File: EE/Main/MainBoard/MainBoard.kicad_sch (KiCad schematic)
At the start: 0 parts

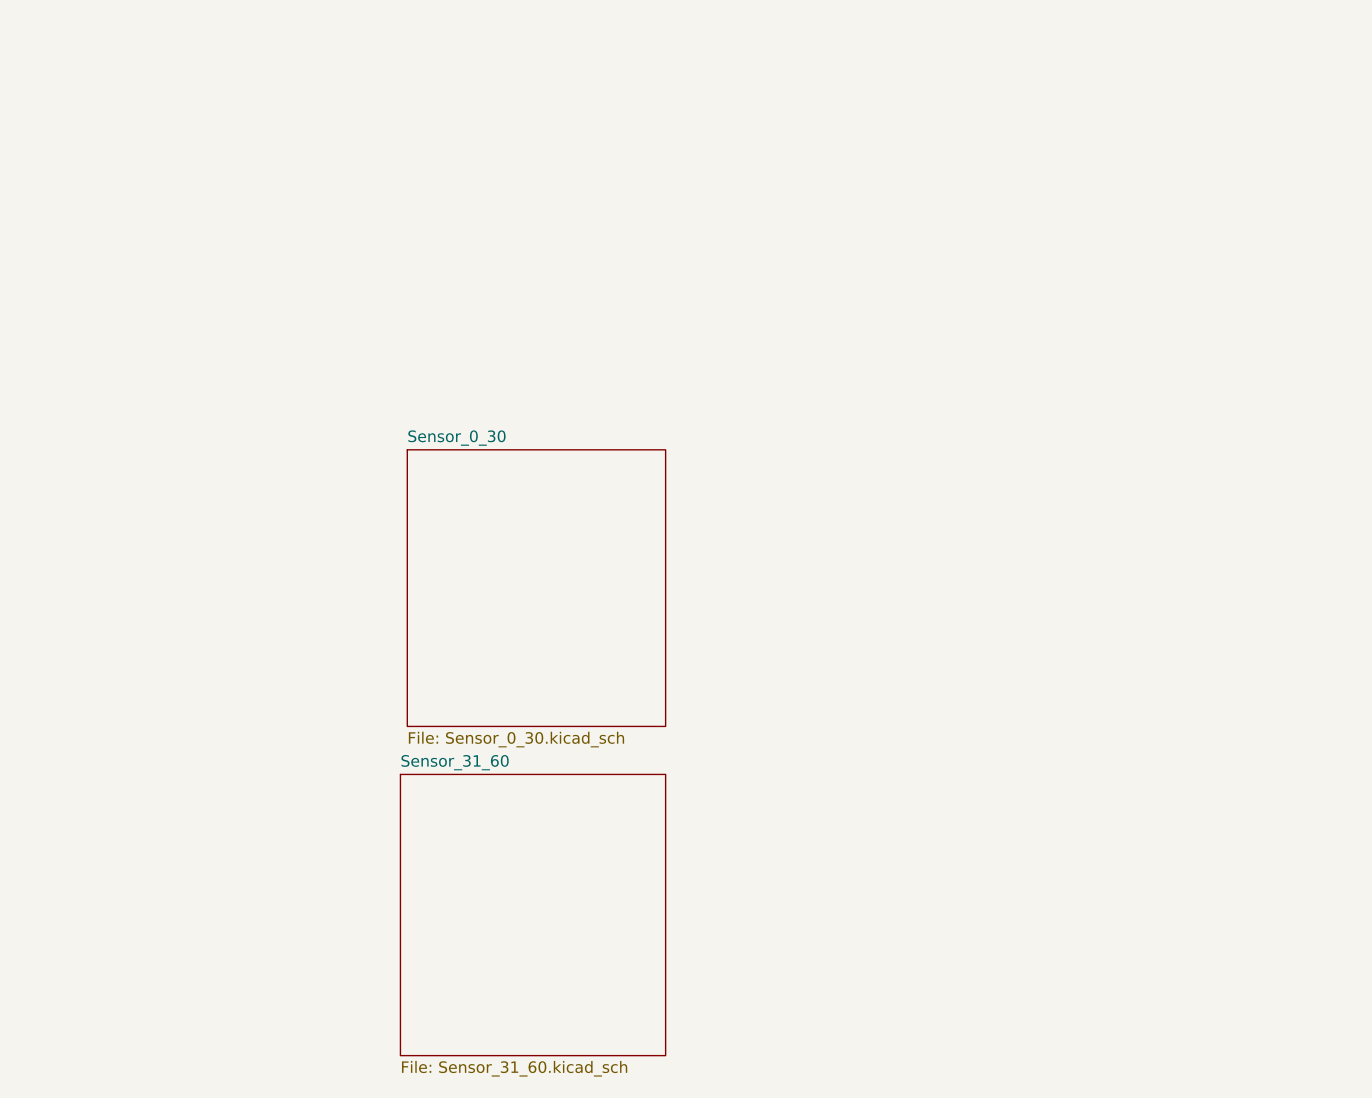
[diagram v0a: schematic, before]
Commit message: Sensors attached to mainboard
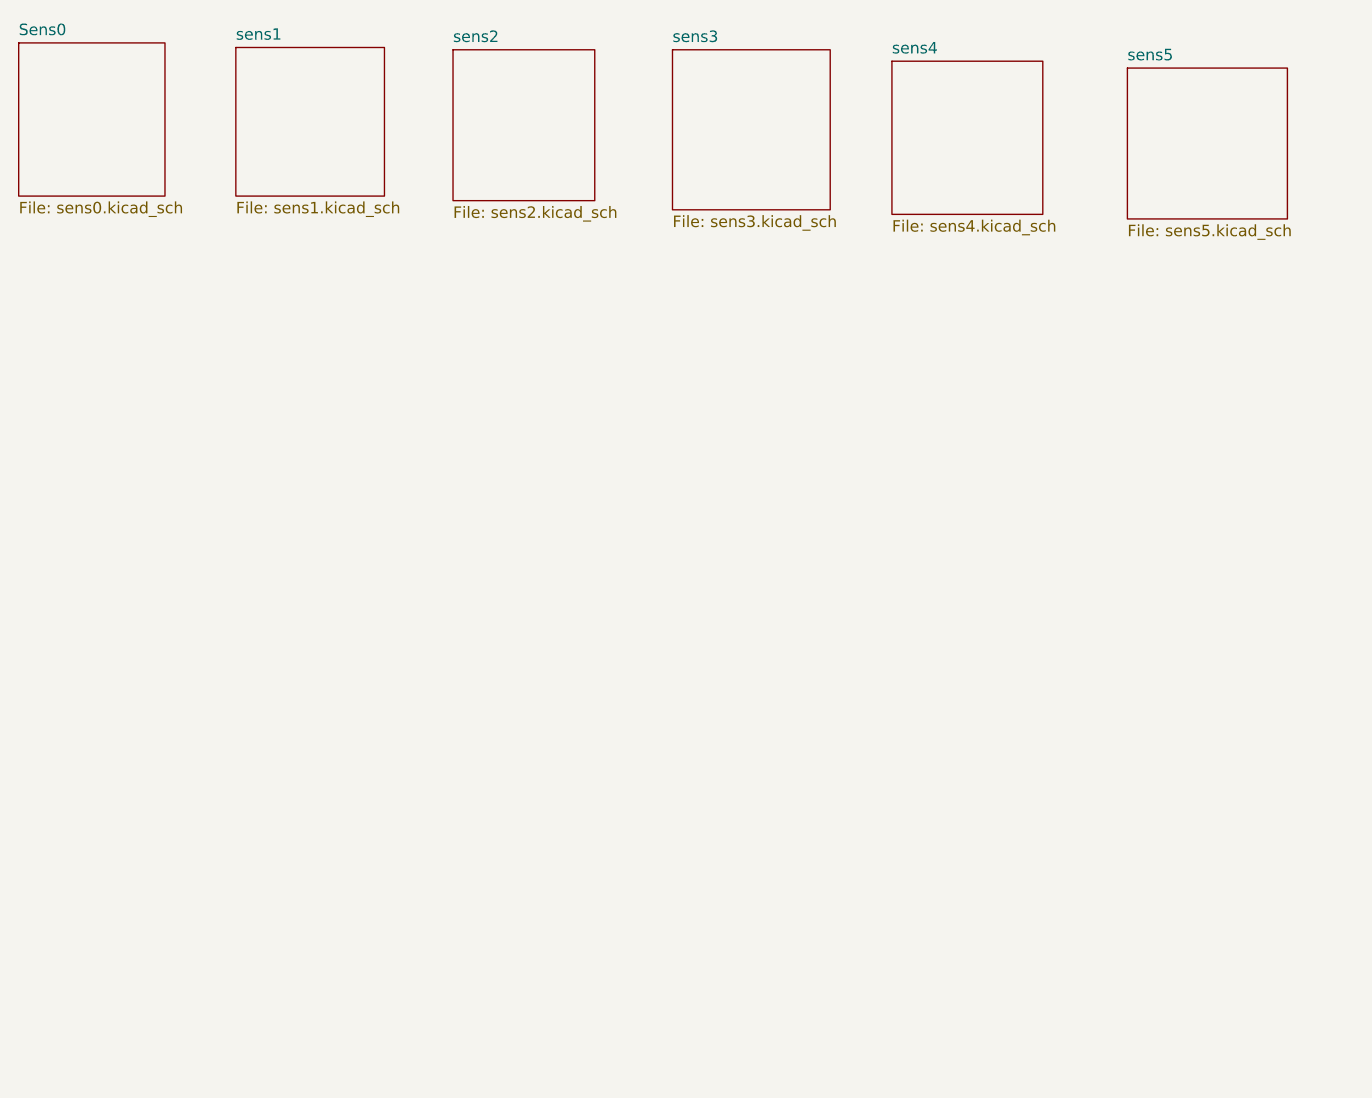
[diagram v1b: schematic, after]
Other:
- removed sheet Sensor_0_30
- removed sheet Sensor_31_60
- added sheet Sens0 (sens0.kicad_sch)
- added sheet sens1 (sens1.kicad_sch)
- added sheet sens2 (sens2.kicad_sch)
- added sheet sens3 (sens3.kicad_sch)
- added sheet sens4 (sens4.kicad_sch)
- added sheet sens5 (sens5.kicad_sch)

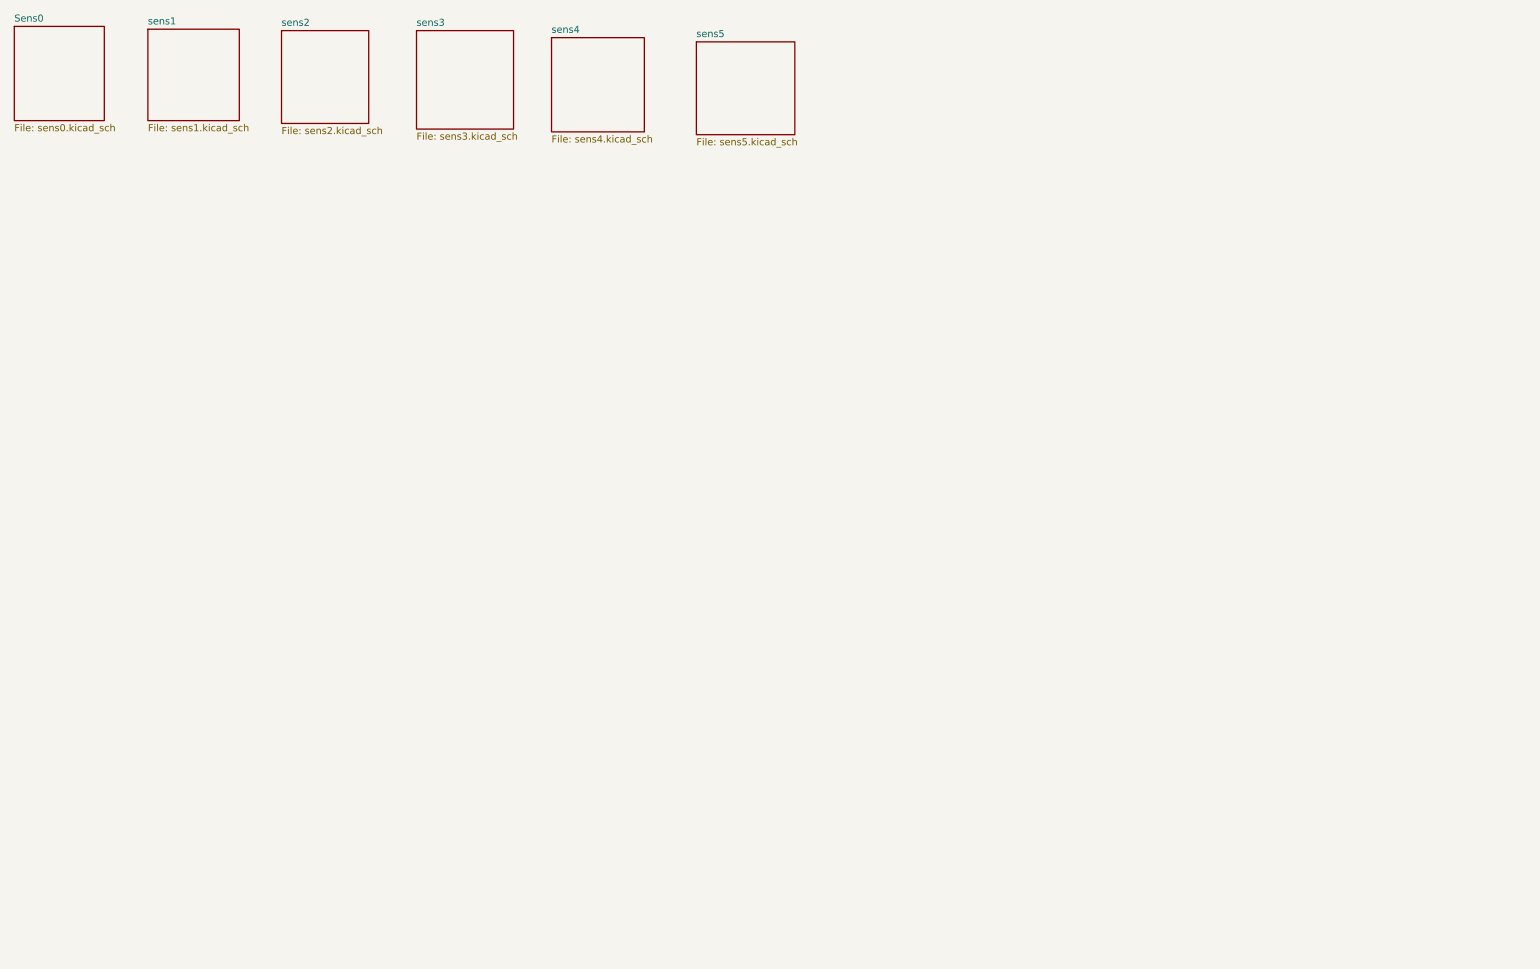
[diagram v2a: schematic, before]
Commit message: WIP - Moving Sensor to IO Expander
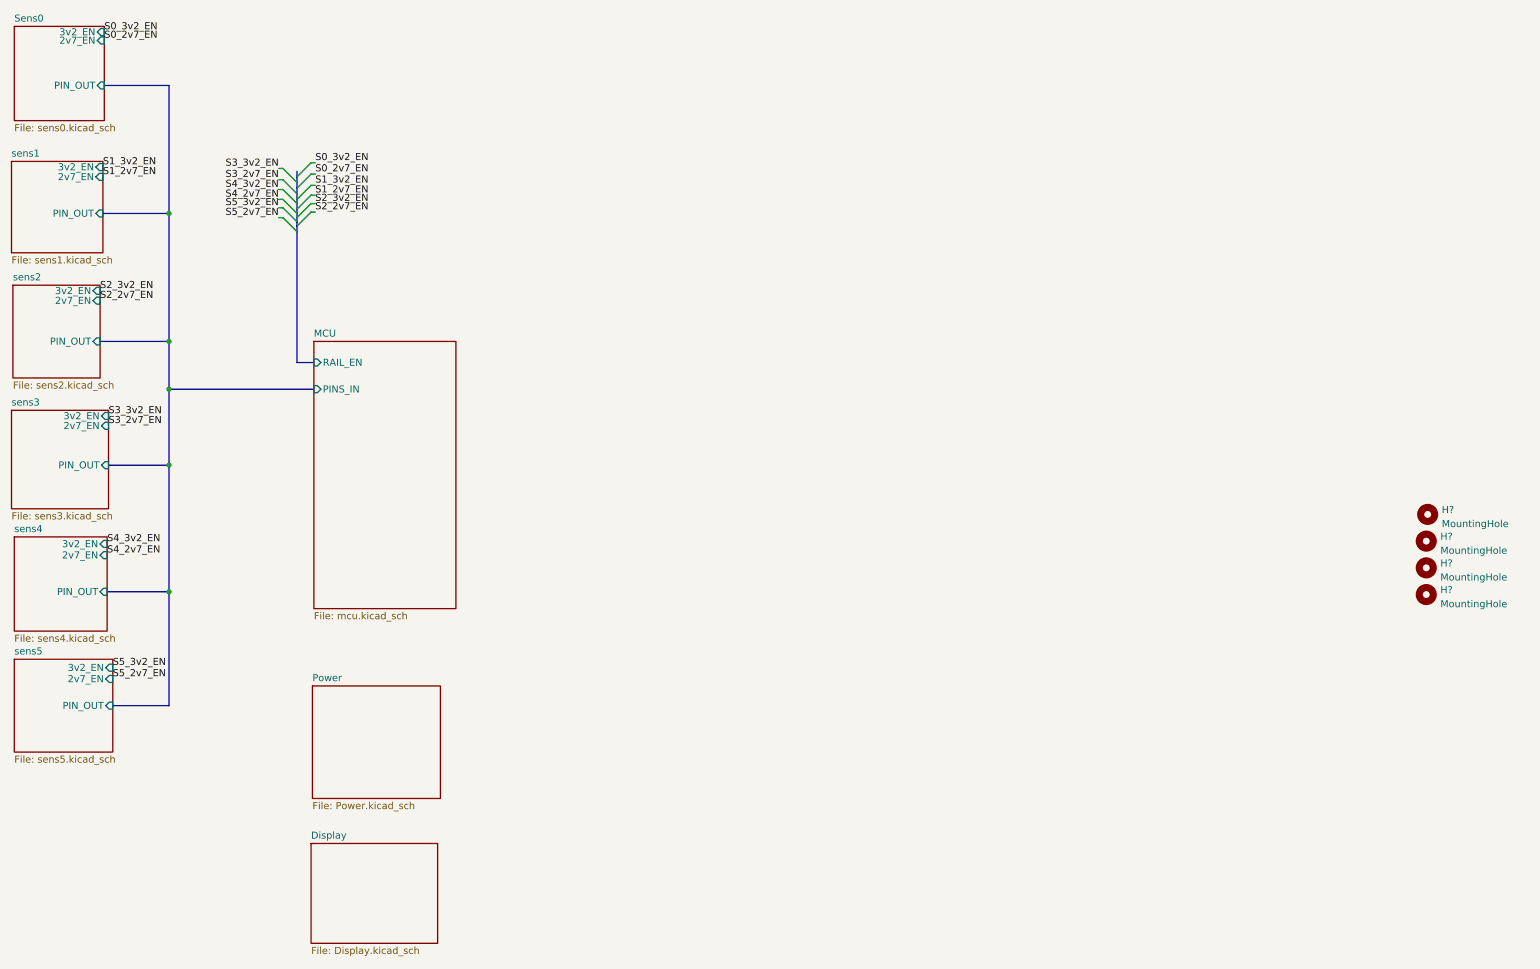
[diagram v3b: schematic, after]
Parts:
- added H? (x4): MountingHole, MountingHole:MountingHole_2.5mm, symbol Mechanical:MountingHole
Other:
- added sheet Display (Display.kicad_sch)
- added sheet MCU (mcu.kicad_sch)
- added sheet Power (Power.kicad_sch)
- sheet Sens0 ports: added 2v7_EN, 3v2_EN, PIN_OUT; removed none
- sheet sens1 ports: added 2v7_EN, 3v2_EN, PIN_OUT; removed none
- sheet sens2 ports: added 2v7_EN, 3v2_EN, PIN_OUT; removed none
- sheet sens3 ports: added 2v7_EN, 3v2_EN, PIN_OUT; removed none
- sheet sens4 ports: added 2v7_EN, 3v2_EN, PIN_OUT; removed none
- sheet sens5 ports: added 2v7_EN, 3v2_EN, PIN_OUT; removed none

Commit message: Updated layout, and placement for main board
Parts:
- gave numbers to parts that had none: 4
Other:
- sheet Display ports: added A_EN, B_EN, C_EN, D1_G_EN, D1_R_EN, D2_G_EN, D2_R_EN, D_EN, E_EN, F_EN, G_EN; removed none
- sheet MCU ports: added A_EN, B_EN, C_EN, D1_G_EN, D1_R_EN, D2_G_EN, D2_R_EN, D_EN, E_EN, F_EN, G_EN, SCL, SDA; removed PINS_IN, RAIL_EN
- sheet Sens0 ports: added SCL, SDA; removed 2v7_EN, 3v2_EN, PIN_OUT
- sheet sens1 ports: added SCL, SDA; removed 2v7_EN, 3v2_EN, PIN_OUT
- sheet sens2 ports: added SCL, SDA; removed 2v7_EN, 3v2_EN, PIN_OUT
- sheet sens3 ports: added SCL, SDA; removed 2v7_EN, 3v2_EN, PIN_OUT
- sheet sens4 ports: added SCL, SDA; removed 2v7_EN, 3v2_EN, PIN_OUT
- sheet sens5 ports: added SCL, SDA; removed 2v7_EN, 3v2_EN, PIN_OUT
- moved on the sheet: H13, H14, H15, H16

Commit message: First pass Finalized Layout. Pending Sensing board changes.
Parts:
- removed H13, H14, H15, H16: MountingHole, MountingHole:MountingHole_2.5mm, symbol Mechanical:MountingHole
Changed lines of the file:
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@@
     (effects (font (size 1.27 1.27)) (justify right bottom))
-  )
-  (symbol (lib_id "Mechanical:MountingHole") (at 181.61 116.078 0) (unit 1)
-    (in_bom yes) (on_board yes) (fields_autoplaced)
-    (property "Reference" "H14" (id 0) (at 184.15 115.2433 0)
-      (effects (font (size 1.27 1.27)) (justify left))
-    )
-    (property "Value" "MountingHole" (id 1) (at 184.15 117.7802 0)
-      (effects (font (size 1.27 1.27)) (justify left))
-    )
-    (property "Footprint" "MountingHole:MountingHole_2.5mm" (id 2) (at 181.61 116.078 0)
-      (effects (font (size 1.27 1.27)) hide)
-    )
-    (property "Datasheet" "~" (id 3) (at 181.61 116.078 0)
-      (effects (font (size 1.27 1.27)) hide)
-    )
-  )
-  (symbol (lib_id "Mechanical:MountingHole") (at 181.61 120.904 0) (unit 1)
-    (in_bom yes) (on_board yes) (fields_autoplaced)
-    (property "Reference" "H15" (id 0) (at 184.15 120.0693 0)
-      (effects (font (size 1.27 1.27)) (justify left))
-    )
-    (property "Value" "MountingHole" (id 1) (at 184.15 122.6062 0)
-      (effects (font (size 1.27 1.27)) (justify left))
-    )
-    (property "Footprint" "MountingHole:MountingHole_2.5mm" (id 2) (at 181.61 120.904 0)
-      (effects (font (size 1.27 1.27)) hide)
-    )
-    (property "Datasheet" "~" (id 3) (at 181.61 120.904 0)
-      (effects (font (size 1.27 1.27)) hide)
-    )
-  )
-  (symbol (lib_id "Mechanical:MountingHole") (at 181.61 111.252 0) (unit 1)
-    (in_bom yes) (on_board yes) (fields_autoplaced)
-    (property "Reference" "H13" (id 0) (at 184.15 110.4173 0)
-      (effects (font (size 1.27 1.27)) (justify left))
-    )
-    (property "Value" "MountingHole" (id 1) (at 184.15 112.9542 0)
-      (effects (font (size 1.27 1.27)) (justify left))
-    )
-    (property "Footprint" "MountingHole:MountingHole_2.5mm" (id 2) (at 181.61 111.252 0)
-      (effects (font (size 1.27 1.27)) hide)
-    )
-    (property "Datasheet" "~" (id 3) (at 181.61 111.252 0)
-      (effects (font (size 1.27 1.27)) hide)
-    )
-  )
-  (symbol (lib_id "Mechanical:MountingHole") (at 181.864 106.426 0) (unit 1)
-    (in_bom yes) (on_board yes) (fields_autoplaced)
-    (property "Reference" "H16" (id 0) (at 184.404 105.5913 0)
-      (effects (font (size 1.27 1.27)) (justify left))
-    )
-    (property "Value" "MountingHole" (id 1) (at 184.404 108.1282 0)
-      (effects (font (size 1.27 1.27)) (justify left))
-    )
-    (property "Footprint" "MountingHole:MountingHole_2.5mm" (id 2) (at 181.864 106.426 0)
-      (effects (font (size 1.27 1.27)) hide)
-    )
-    (property "Datasheet" "~" (id 3) (at 181.864 106.426 0)
-      (effects (font (size 1.27 1.27)) hide)
-    )
   )
   (sheet (at 69.596 73.914) (size 25.654 48.26) (fields_autoplaced)
@@
       (reference "H12") (unit 1) (value "MountingHole") (footprint "MountingHole:MountingHole_2.5mm")
     )
-    (path "/8112631e-48af-41df-b687-cfed77ad01f8"
-      (reference "H13") (unit 1) (value "MountingHole") (footprint "MountingHole:MountingHole_2.5mm")
-    )
-    (path "/3bae4020-79f4-48a4-a1e2-5e81454f7ed9"
-      (reference "H14") (unit 1) (value "MountingHole") (footprint "MountingHole:MountingHole_2.5mm")
-    )
-    (path "/6ad99c37-29b1-408c-b9fc-41eaeaf45fdb"
-      (reference "H15") (unit 1) (value "MountingHole") (footprint "MountingHole:MountingHole_2.5mm")
-    )
-    (path "/f20fd224-55d9-4c9e-ad9f-b6ce8e565db2"
-      (reference "H16") (unit 1) (value "MountingHole") (footprint "MountingHole:MountingHole_2.5mm")
-    )
     (path "/3c0cf0fe-1230-4a73-9d8b-47e10780e7d7/f809c2a5-de1d-469d-89e4-a0c654f42183"

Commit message: Random Check in
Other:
- sheet Display ports: added DISPLAY_DIN, V_DISPLAY; removed A_EN, B_EN, C_EN, D1_G_EN, D1_R_EN, D2_G_EN, D2_R_EN, D_EN, E_EN, F_EN, G_EN
- sheet MCU ports: added DISPLAY_DIN; removed A_EN, B_EN, C_EN, D1_G_EN, D1_R_EN, D2_G_EN, D2_R_EN, D_EN, E_EN, F_EN, G_EN
